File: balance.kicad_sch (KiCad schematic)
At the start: 18 parts, among them Q10 AO3401A, Q5 AO3401A, Q6 AO3400A, Q7 AO3400A, Q8 AO3401A, Q9 AO3400A

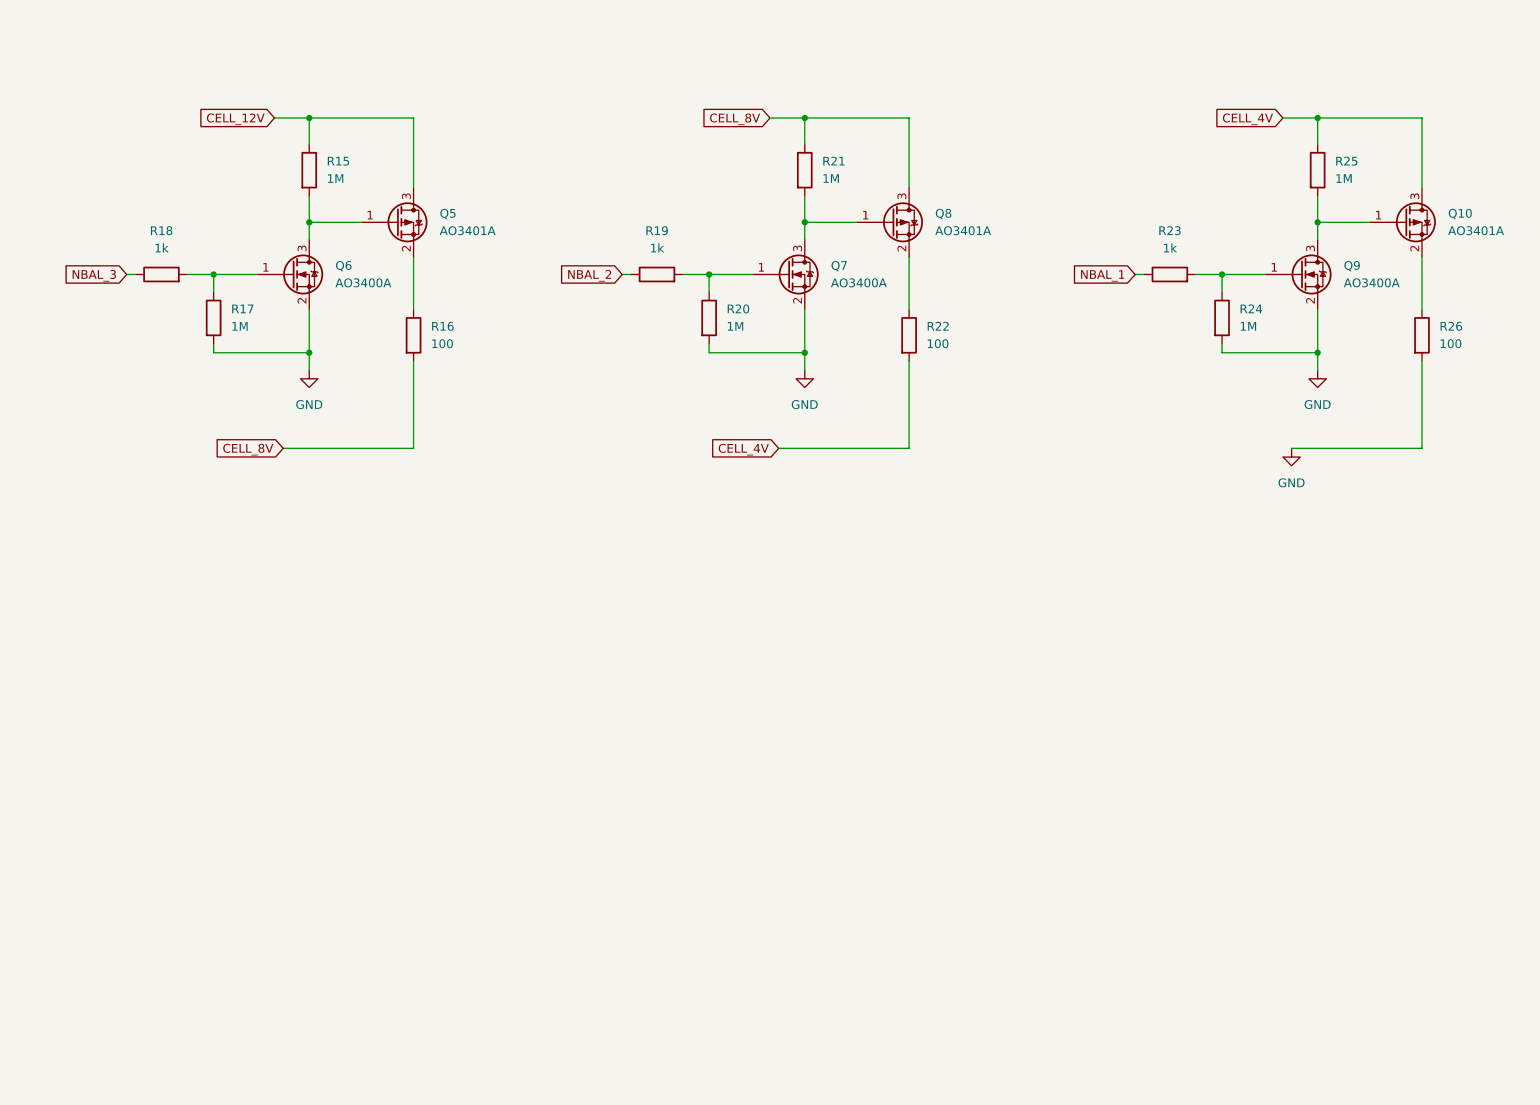
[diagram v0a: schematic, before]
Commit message: Smaller diodes, more work
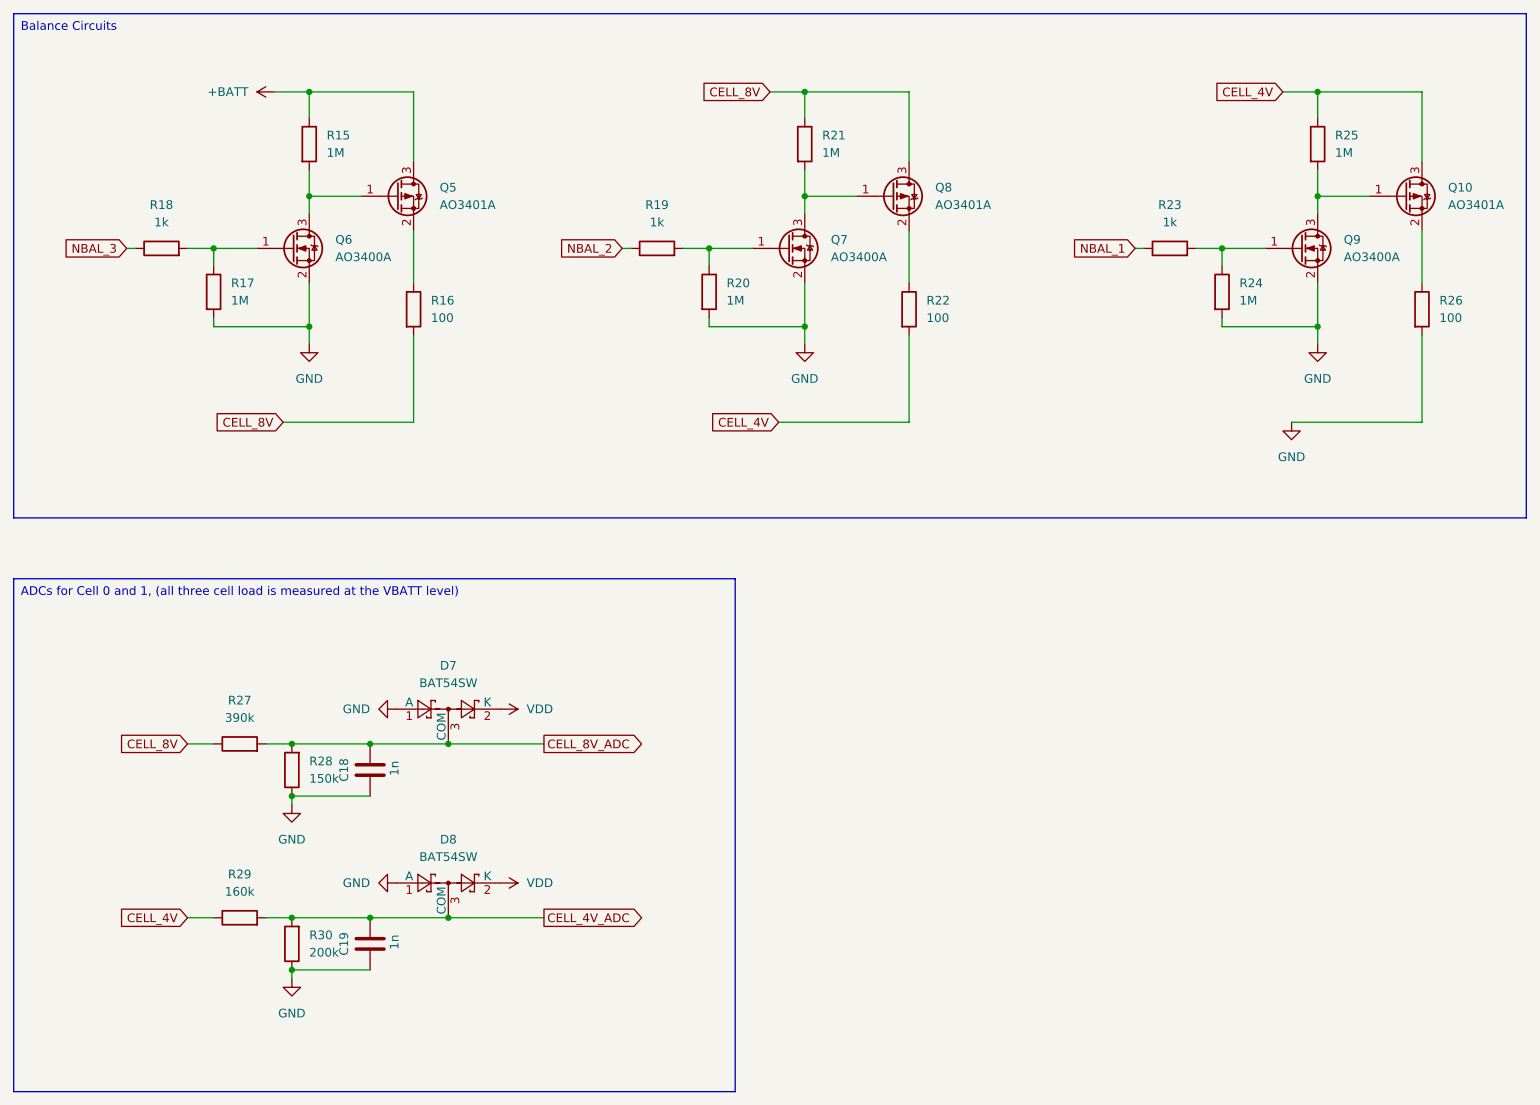
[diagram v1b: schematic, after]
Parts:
- added C18, C19: 1n, Capacitor_SMD:C_0603_1608Metric, symbol Device:C
- added D7, D8: BAT54SW, Package_TO_SOT_SMD:SOT-323_SC-70, symbol Diode:BAT54SW
- added R27: 390k, Resistor_SMD:R_0603_1608Metric, symbol Device:R
- added R28: 150k, Resistor_SMD:R_0603_1608Metric, symbol Device:R
- added R29: 160k, Resistor_SMD:R_0603_1608Metric, symbol Device:R
- added R30: 200k, Resistor_SMD:R_0603_1608Metric, symbol Device:R
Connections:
- net CELL_4V: now also R29.1
- net CELL_8V: now also R27.1
- net GND: now also C18.2, C19.2, D7.1 (A), D8.1 (A), R28.1, R30.1
- net CELL_12V renamed +BATT
- new net CELL_4V_ADC: C19.1, D8.3 (COM), R29.2, R30.2
- new net CELL_8V_ADC: C18.1, D7.3 (COM), R27.2, R28.2
- new net VDD: D7.2 (K), D8.2 (K)
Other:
- moved on the sheet: Q10, Q5, Q6, Q7, Q8, Q9, R15, R16, R17, R18, R19, R20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

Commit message: Some more placement
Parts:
- removed Q6, Q7, Q9: AO3400A, Package_TO_SOT_SMD:SOT-23, symbol Transistor_FET:AO3400A
- added Q11, Q6, Q7: 2N7002, Package_TO_SOT_SMD:SOT-323_SC-70, symbol Transistor_FET:2N7002
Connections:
- net GND: now also Q11.2 (S), Q6.2 (S), Q7.2 (S)
- net at R23.2, R24.1: now also Q7.1 (G)
- net at Q10.1 (G), R25.2: now also Q7.3 (D)
- net at R17.1, R18.2: now also Q11.1 (G)
- net at R19.2, R20.1: now also Q6.1 (G)
- net at Q8.1 (G), R21.2: now also Q6.3 (D)
- net at Q5.1 (G), R15.2: now also Q11.3 (D)
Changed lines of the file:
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@@
-	)
-	(symbol
-		(lib_id "Transistor_FET:AO3400A")
-		(at 226.06 59.69 0)
-		(unit 1)
-		(exclude_from_sim no)
-		(in_bom yes)
-		(on_board yes)
-		(dnp no)
-		(fields_autoplaced yes)
-		(property "Reference" "Q9"
-			(at 232.41 58.4199 0)
-			(effects
-				(font
-					(size 1.27 1.27)
-				)
-				(justify left)
-			)
-		)
-		(property "Value" "AO3400A"
-			(at 232.41 60.9599 0)
-			(effects
-				(font
-					(size 1.27 1.27)
-				)
-				(justify left)
-			)
-		)
-		(property "Footprint" "Package_TO_SOT_SMD:SOT-23"
-			(at 231.14 61.595 0)
-			(effects
-				(font
-					(size 1.27 1.27)
-					(italic yes)
-				)
-				(justify left)
-				(hide yes)
-			)
-		)
-		(property "Datasheet" "http://www.aosmd.com/pdfs/datasheet/AO3400A.pdf"
-			(at 231.14 63.5 0)
-			(effects
-				(font
-					(size 1.27 1.27)
-				)
-				(justify left)
-				(hide yes)
-			)
-		)
-		(property "Description" "30V Vds, 5.7A Id, N-Channel MOSFET, SOT-23"
-			(at 226.06 59.69 0)
-			(effects
-				(font
-					(size 1.27 1.27)
-				)
-				(hide yes)
-			)
-		)
-		(pin "1"
-		)
-		(pin "2"
-		)
-		(pin "3"
-		)
-		(instances
-			(project "JPBms2"
-				(path "/d86e471c-a8be-422d-a5d1-5a4699b7b766/220685a5-608c-4c12-9441-6825efcef07c"
-					(reference "Q9")
-					(unit 1)
-				)
-			)
-		)
 	)
 	(symbol
@@
 	)
 	(symbol
+		(lib_id "Transistor_FET:2N7002")
+		(at 151.13 59.69 0)
+		(unit 1)
+		(exclude_from_sim no)
+		(in_bom yes)
+		(on_board yes)
+		(dnp no)
+		(fields_autoplaced yes)
+		(property "Reference" "Q6"
+			(at 157.48 58.4199 0)
+			(effects
+				(font
+					(size 1.27 1.27)
+				)
+				(justify left)
+			)
+		)
+		(property "Value" "2N7002"
+			(at 157.48 60.9599 0)
+			(effects
+				(font
+					(size 1.27 1.27)
+				)
+				(justify left)
+			)
+		)
+		(property "Footprint" "Package_TO_SOT_SMD:SOT-323_SC-70"
+			(at 156.21 61.595 0)
+			(effects
+				(font
+					(size 1.27 1.27)
+					(italic yes)
+				)
+				(justify left)
+				(hide yes)
+			)
+		)
+		(property "Datasheet" "https://www.onsemi.com/pub/Collateral/NDS7002A-D.PDF"
+			(at 156.21 63.5 0)
+			(effects
+				(font
+					(size 1.27 1.27)
+				)
+				(justify left)
+				(hide yes)
+			)
+		)
+		(property "Description" "0.115A Id, 60V Vds, N-Channel MOSFET, SOT-23"
+			(at 151.13 59.69 0)
+			(effects
+				(font
+					(size 1.27 1.27)
+				)
+				(hide yes)
+			)
+		)
+		(pin "1"
+		)
+		(pin "3"
+		)
+		(pin "2"
+		)
+		(instances
+			(project "JPBms2"
+				(path "/d86e471c-a8be-422d-a5d1-5a4699b7b766/220685a5-608c-4c12-9441-6825efcef07c"
+					(reference "Q6")
+					(unit 1)
+				)
+			)
+		)
+	)
+	(symbol
 		(lib_id "Device:R")
 		(at 78.74 135.89 180)
@@
 	)
 	(symbol
-		(lib_id "Transistor_FET:AO3400A")
-		(at 151.13 59.69 0)
-		(unit 1)
-		(exclude_from_sim no)
-		(in_bom yes)
-		(on_board yes)
-		(dnp no)
-		(fields_autoplaced yes)
-		(property "Reference" "Q7"
-			(at 157.48 58.4199 0)
-			(effects
-				(font
-					(size 1.27 1.27)
-				)
-				(justify left)
-			)
-		)
-		(property "Value" "AO3400A"
-			(at 157.48 60.9599 0)
-			(effects
-				(font
-					(size 1.27 1.27)
-				)
-				(justify left)
-			)
-		)
-		(property "Footprint" "Package_TO_SOT_SMD:SOT-23"
-			(at 156.21 61.595 0)
-			(effects
-				(font
-					(size 1.27 1.27)
-					(italic yes)
-				)
-				(justify left)
-				(hide yes)
-			)
-		)
-		(property "Datasheet" "http://www.aosmd.com/pdfs/datasheet/AO3400A.pdf"
-			(at 156.21 63.5 0)
-			(effects
-				(font
-					(size 1.27 1.27)
-				)
-				(justify left)
-				(hide yes)
-			)
-		)
-		(property "Description" "30V Vds, 5.7A Id, N-Channel MOSFET, SOT-23"
-			(at 151.13 59.69 0)
-			(effects
-				(font
-					(size 1.27 1.27)
-				)
-				(hide yes)
-			)
-		)
-		(pin "1"
-		)
-		(pin "2"
-		)
-		(pin "3"
-		)
-		(instances
-			(project "JPBms2"
-				(path "/d86e471c-a8be-422d-a5d1-5a4699b7b766/220685a5-608c-4c12-9441-6825efcef07c"
-					(reference "Q7")
-					(unit 1)
-				)
-			)
-		)
-	)
-	(symbol
 		(lib_id "Device:R")
 		(at 214.63 66.04 0)
@@
 	)
 	(symbol
+		(lib_id "Transistor_FET:2N7002")
+		(at 78.74 59.69 0)
+		(unit 1)
+		(exclude_from_sim no)
+		(in_bom yes)
+		(on_board yes)
+		(dnp no)
+		(fields_autoplaced yes)
+		(property "Reference" "Q11"
+			(at 85.09 58.4199 0)
+			(effects
+				(font
+					(size 1.27 1.27)
+				)
+				(justify left)
+			)
+		)
+		(property "Value" "2N7002"
+			(at 85.09 60.9599 0)
+			(effects
+				(font
+					(size 1.27 1.27)
+				)
+				(justify left)
+			)
+		)
+		(property "Footprint" "Package_TO_SOT_SMD:SOT-323_SC-70"
+			(at 83.82 61.595 0)
+			(effects
+				(font
+					(size 1.27 1.27)
+					(italic yes)
+				)
+				(justify left)
+				(hide yes)
+			)
+		)
+		(property "Datasheet" "https://www.onsemi.com/pub/Collateral/NDS7002A-D.PDF"
+			(at 83.82 63.5 0)
+			(effects
+				(font
+					(size 1.27 1.27)
+				)
+				(justify left)
+				(hide yes)
+			)
+		)
+		(property "Description" "0.115A Id, 60V Vds, N-Channel MOSFET, SOT-23"
+			(at 78.74 59.69 0)
+			(effects
+				(font
+					(size 1.27 1.27)
+				)
+				(hide yes)
+			)
+		)
+		(pin "1"
+		)
+		(pin "3"
+		)
+		(pin "2"
+		)
+		(instances
+			(project "JPBms2"
+				(path "/d86e471c-a8be-422d-a5d1-5a4699b7b766/220685a5-608c-4c12-9441-6825efcef07c"
+					(reference "Q11")
+					(unit 1)
+				)
+			)
+		)
+	)
+	(symbol
 		(lib_id "Device:R")
 		(at 78.74 161.29 180)
@@
 	)
 	(symbol
+		(lib_id "Transistor_FET:2N7002")
+		(at 226.06 59.69 0)
+		(unit 1)
+		(exclude_from_sim no)
+		(in_bom yes)
+		(on_board yes)
+		(dnp no)
+		(fields_autoplaced yes)
+		(property "Reference" "Q7"
+			(at 232.41 58.4199 0)
+			(effects
+				(font
+					(size 1.27 1.27)
+				)
+				(justify left)
+			)
+		)
+		(property "Value" "2N7002"
+			(at 232.41 60.9599 0)
+			(effects
+				(font
+					(size 1.27 1.27)
+				)
+				(justify left)
+			)
+		)
+		(property "Footprint" "Package_TO_SOT_SMD:SOT-323_SC-70"
+			(at 231.14 61.595 0)
+			(effects
+				(font
+					(size 1.27 1.27)
+					(italic yes)
+				)
+				(justify left)
+				(hide yes)
+			)
+		)
+		(property "Datasheet" "https://www.onsemi.com/pub/Collateral/NDS7002A-D.PDF"
+			(at 231.14 63.5 0)
+			(effects
+				(font
+					(size 1.27 1.27)
+				)
+				(justify left)
+				(hide yes)
+			)
+		)
+		(property "Description" "0.115A Id, 60V Vds, N-Channel MOSFET, SOT-23"
+			(at 226.06 59.69 0)
+			(effects
+				(font
+					(size 1.27 1.27)
+				)
+				(hide yes)
+			)
+		)
+		(pin "1"
+		)
+		(pin "3"
+		)
+		(pin "2"
+		)
+		(instances
+			(project "JPBms2"
+				(path "/d86e471c-a8be-422d-a5d1-5a4699b7b766/220685a5-608c-4c12-9441-6825efcef07c"
+					(reference "Q7")
+					(unit 1)
+				)
+			)
+		)
+	)
+	(symbol
 		(lib_id "Device:R")
 		(at 243.84 68.58 0)
@@
 					(unit 1)
 				)
-			)
-		)
-	)
-	(symbol
-		(lib_id "Transistor_FET:AO3400A")
-		(at 78.74 59.69 0)
-		(unit 1)
-		(exclude_from_sim no)
-		(in_bom yes)
-		(on_board yes)
-		(dnp no)
-		(fields_autoplaced yes)
-		(property "Reference" "Q6"
-			(at 85.09 58.4199 0)
-			(effects
-				(font
-					(size 1.27 1.27)
-				)
-				(justify left)
-			)
-		)
-		(property "Value" "AO3400A"
-			(at 85.09 60.9599 0)
-			(effects
-				(font
-					(size 1.27 1.27)
-				)
-				(justify left)
-			)
-		)
-		(property "Footprint" "Package_TO_SOT_SMD:SOT-23"
-			(at 83.82 61.595 0)
-			(effects
-				(font
-					(size 1.27 1.27)
-					(italic yes)
-				)
-				(justify left)
-				(hide yes)
-			)
-		)
-		(property "Datasheet" "http://www.aosmd.com/pdfs/datasheet/AO3400A.pdf"
-			(at 83.82 63.5 0)
-			(effects
-				(font
-					(size 1.27 1.27)
-				)
-				(justify left)
-				(hide yes)
-			)
-		)
-		(property "Description" "30V Vds, 5.7A Id, N-Channel MOSFET, SOT-23"
-			(at 78.74 59.69 0)
-			(effects
-				(font
-					(size 1.27 1.27)
-				)
-				(hide yes)
-			)
-		)
-		(pin "1"
-		)
-		(pin "2"
-		)
-		(pin "3"
-		)
-		(instances
-			(project "JPBms2"
-				(path "/d86e471c-a8be-422d-a5d1-5a4699b7b766/220685a5-608c-4c12-9441-6825efcef07c"
-					(reference "Q6")
-					(unit 1)
-				)

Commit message: Assigning PNs
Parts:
- C18, C19: LCSC_Code (none) -> C1588
- D7, D8: LCSC_Code (none) -> C78606
- Q10, Q5, Q8: LCSC_Code (none) -> C15127
- Q11, Q6, Q7: LCSC_Code (none) -> C5224210
- R15, R17, R20, R21, R24, R25: LCSC_Code (none) -> C22935
- R16, R22, R26: LCSC_Code (none) -> C17408
- R18, R19, R23: LCSC_Code (none) -> C21190
- R27: LCSC_Code (none) -> C23150
- R28: LCSC_Code (none) -> C22807
- R29: value 160k -> 150k; LCSC_Code (none) -> C22807
- R30: LCSC_Code (none) -> C25811
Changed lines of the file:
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@@
+			)
+		)
+		(property "LCSC_Code" "C78606"
+			(at 101.6 127 0)
+			(effects
+				(font
+					(size 1.27 1.27)
+				)
+				(hide yes)
 			)
 		)
@@
 			)
 		)
+		(property "LCSC_Code" "C22935"
+			(at 67.31 66.04 0)
+			(effects
+				(font
+					(size 1.27 1.27)
+				)
+				(hide yes)
+			)
+		)
 		(pin "1"
 		)
@@
 			)
 		)
+		(property "LCSC_Code" "C5224210"
+			(at 151.13 59.69 0)
+			(effects
+				(font
+					(size 1.27 1.27)
+				)
+				(hide yes)
+			)
+		)
 		(pin "1"
 		)
@@
 			)
 		)
+		(property "LCSC_Code" "C22807"
+			(at 78.74 135.89 0)
+			(effects
+				(font
+					(size 1.27 1.27)
+				)
+				(hide yes)
+			)
+		)
 		(pin "2"
 		)
@@
 			)
 		)
+		(property "LCSC_Code" "C22935"
+			(at 214.63 66.04 0)
+			(effects
+				(font
+					(size 1.27 1.27)
+				)
+				(hide yes)
+			)
+		)
 		(pin "1"
 		)
@@
 			)
 		)
+		(property "LCSC_Code" "C21190"
+			(at 207.01 59.69 0)
+			(effects
+				(font
+					(size 1.27 1.27)
+				)
+				(hide yes)
+			)
+		)
 		(pin "1"
 		)
@@
 			)
 		)
+		(property "LCSC_Code" "C1588"
+			(at 90.17 161.29 0)
+			(effects
+				(font
+					(size 1.27 1.27)
+				)
+				(hide yes)
+			)
+		)
 		(pin "2"
 		)
@@
 			)
 		)
+		(property "LCSC_Code" "C23150"
+			(at 71.12 132.08 0)
+			(effects
+				(font
+					(size 1.27 1.27)
+				)
+				(hide yes)
+			)
+		)
 		(pin "2"
 		)
@@
 			)
 		)
+		(property "LCSC_Code" "C5224210"
+			(at 78.74 59.69 0)
+			(effects
+				(font
+					(size 1.27 1.27)
+				)
+				(hide yes)
+			)
+		)
 		(pin "1"
 		)
@@
 			)
 		)
+		(property "LCSC_Code" "C25811"
+			(at 78.74 161.29 0)
+			(effects
+				(font
+					(size 1.27 1.27)
+				)
+				(hide yes)
+			)
+		)
 		(pin "2"
 		)
@@
 			)
 		)
+		(property "LCSC_Code" "C22935"
+			(at 139.7 66.04 0)
+			(effects
+				(font
+					(size 1.27 1.27)
+				)
+				(hide yes)
+			)
+		)
 		(pin "1"
 		)
@@
 			)
 		)
+		(property "LCSC_Code" "C1588"
+			(at 90.17 135.89 0)
+			(effects
+				(font
+					(size 1.27 1.27)
+				)
+				(hide yes)
+			)
+		)
 		(pin "2"
 		)
@@
 			)
 		)
+		(property "LCSC_Code" "C22935"
+			(at 153.67 44.45 0)
+			(effects
+				(font
+					(size 1.27 1.27)
+				)
+				(hide yes)
+			)
+		)
 		(pin "1"
 		)
@@
 			)
 		)
+		(property "LCSC_Code" "C5224210"
+			(at 226.06 59.69 0)
+			(effects
+				(font
+					(size 1.27 1.27)
+				)
+				(hide yes)
+			)
+		)
 		(pin "1"
 		)
@@
 			)
 		)
+		(property "LCSC_Code" "C17408"
+			(at 243.84 68.58 0)
+			(effects
+				(font
+					(size 1.27 1.27)
+				)
+				(hide yes)
+			)
+		)
 		(pin "1"
 		)
@@
 			)
 		)
+		(property "LCSC_Code" "C78606"
+			(at 101.6 152.4 0)
+			(effects
+				(font
+					(size 1.27 1.27)
+				)
+				(hide yes)
+			)
+		)
 		(pin "1"
 		)
@@
 			)
 		)
+		(property "LCSC_Code" "C22935"
+			(at 81.28 44.45 0)
+			(effects
+				(font
+					(size 1.27 1.27)
+				)
+				(hide yes)
+			)
+		)
 		(pin "1"
 		)
@@
 			)
 		)
+		(property "LCSC_Code" "C21190"
+			(at 132.08 59.69 0)
+			(effects
+				(font
+					(size 1.27 1.27)
+				)
+				(hide yes)
+			)
+		)
 		(pin "1"
 		)
@@
 			)
 		)
+		(property "LCSC_Code" "C21190"
+			(at 59.69 59.69 0)
+			(effects
+				(font
+					(size 1.27 1.27)
+				)
+				(hide yes)
+			)
+		)
 		(pin "1"
 		)
@@
 			)
 		)
+		(property "LCSC_Code" "C17408"
+			(at 168.91 68.58 0)
+			(effects
+				(font
+					(size 1.27 1.27)
+				)
+				(hide yes)
+			)
+		)
 		(pin "1"
 		)
@@
 			)
 		)
+		(property "LCSC_Code" "C15127"
+			(at 93.98 52.07 0)
+			(effects
+				(font
+					(size 1.27 1.27)
+				)
+				(hide yes)
+			)
+		)
 		(pin "3"
 		)
@@
 			)
 		)
+		(property "LCSC_Code" "C17408"
+			(at 96.52 68.58 0)
+			(effects
+				(font
+					(size 1.27 1.27)
+				)
+				(hide yes)
+			)
+		)
 		(pin "1"
 		)
@@
 			)
 		)
+		(property "LCSC_Code" "C15127"
+			(at 166.37 52.07 0)
+			(effects
+				(font
+					(size 1.27 1.27)
+				)
+				(hide yes)
+			)
+		)
 		(pin "3"
 		)
@@
 			)
 		)
+		(property "LCSC_Code" "C15127"
+			(at 241.3 52.07 0)
+			(effects
+				(font
+					(size 1.27 1.27)
+				)
+				(hide yes)
+			)
+		)
 		(pin "3"
 		)
@@
 			)
 		)
-		(property "Value" "160k"
+		(property "Value" "150k"
 			(at 71.12 153.67 90)
 			(effects
@@
 			)
 		)
+		(property "LCSC_Code" "C22807"
+			(at 71.12 157.48 0)
+			(effects
+				(font
+					(size 1.27 1.27)
+				)
+				(hide yes)
+			)
+		)
 		(pin "2"
 		)
@@
 			(at 228.6 44.45 0)
 			(effects
+				(font
+					(size 1.27 1.27)
+				)
+				(hide yes)
+			)
+		)
+		(property "LCSC_Code" "C22935"
+			(at 228.6 44.45 0)
+			(effects

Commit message: sent to jlcpcb
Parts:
- Q11, Q6, Q7: LCSC_Code C5224210 -> C7420322
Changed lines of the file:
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@@
 			)
 		)
-		(property "LCSC_Code" "C5224210"
+		(property "LCSC_Code" "C7420322"
 			(at 151.13 59.69 0)
 			(effects
@@
 			)
 		)
-		(property "LCSC_Code" "C5224210"
+		(property "LCSC_Code" "C7420322"
 			(at 78.74 59.69 0)
 			(effects
@@
 			)
 		)
-		(property "LCSC_Code" "C5224210"
+		(property "LCSC_Code" "C7420322"
 			(at 226.06 59.69 0)
 			(effects
